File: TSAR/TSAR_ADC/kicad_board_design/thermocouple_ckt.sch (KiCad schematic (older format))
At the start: 75 parts, among them U3 AD8495, U4 AD8495, U5 AD8495, U6 AD8495, U7 ADA4062, U8 MCP3424T-E/ST, U9 LM358DR

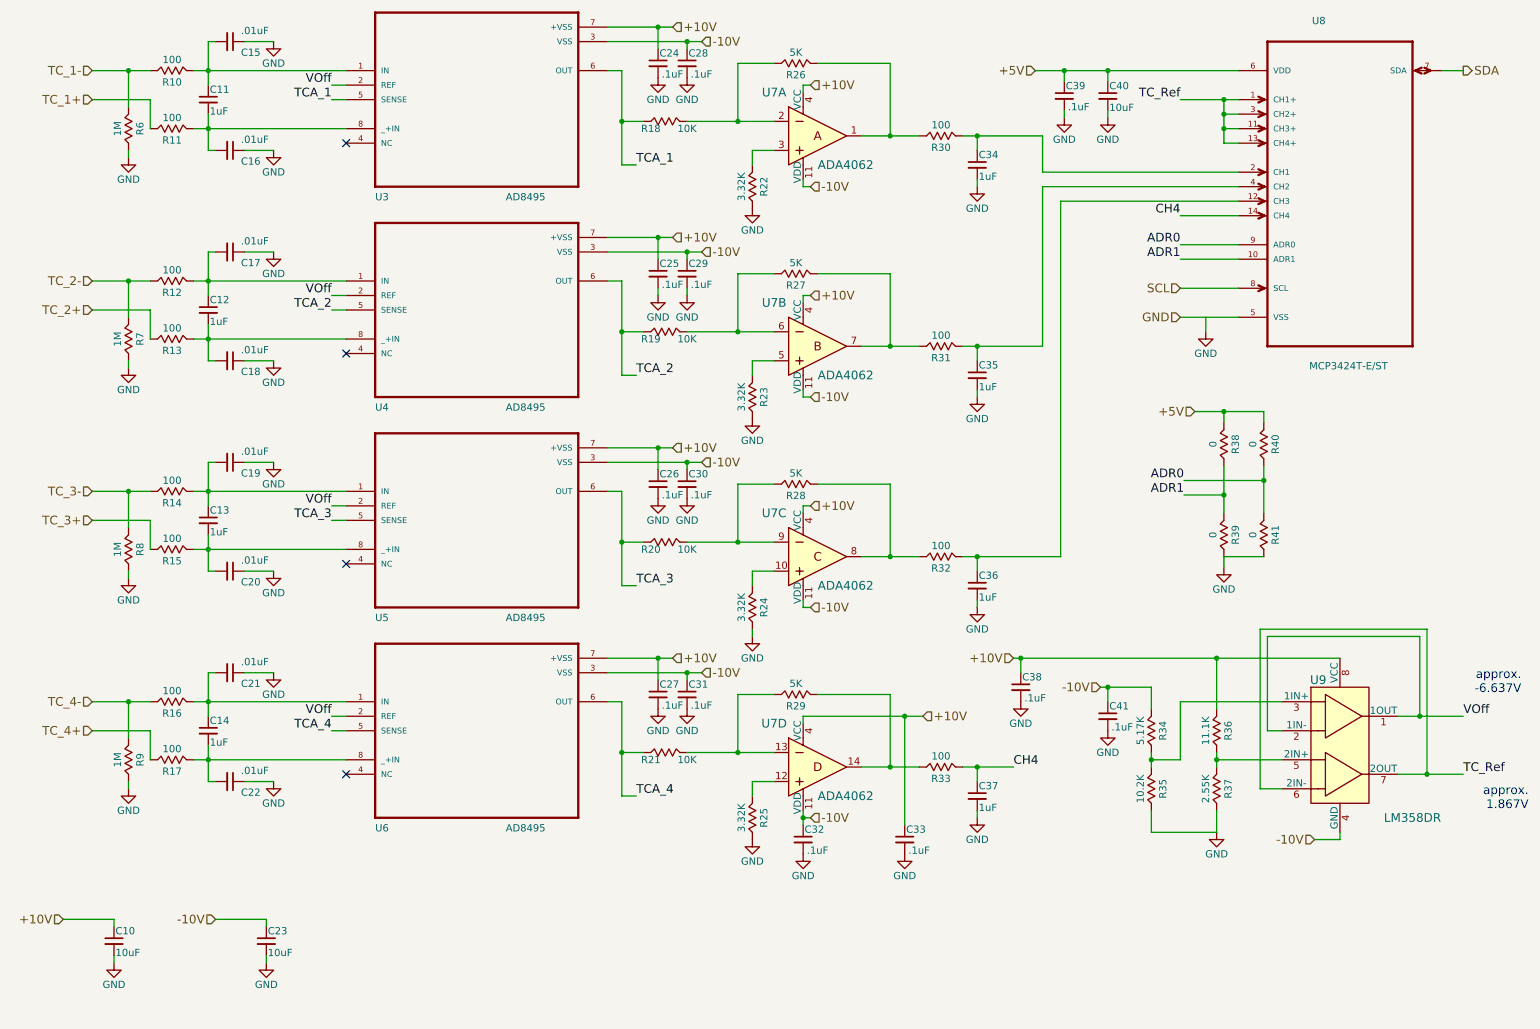
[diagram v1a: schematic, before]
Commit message: Simplify thermocouple signal chain for better worst case.
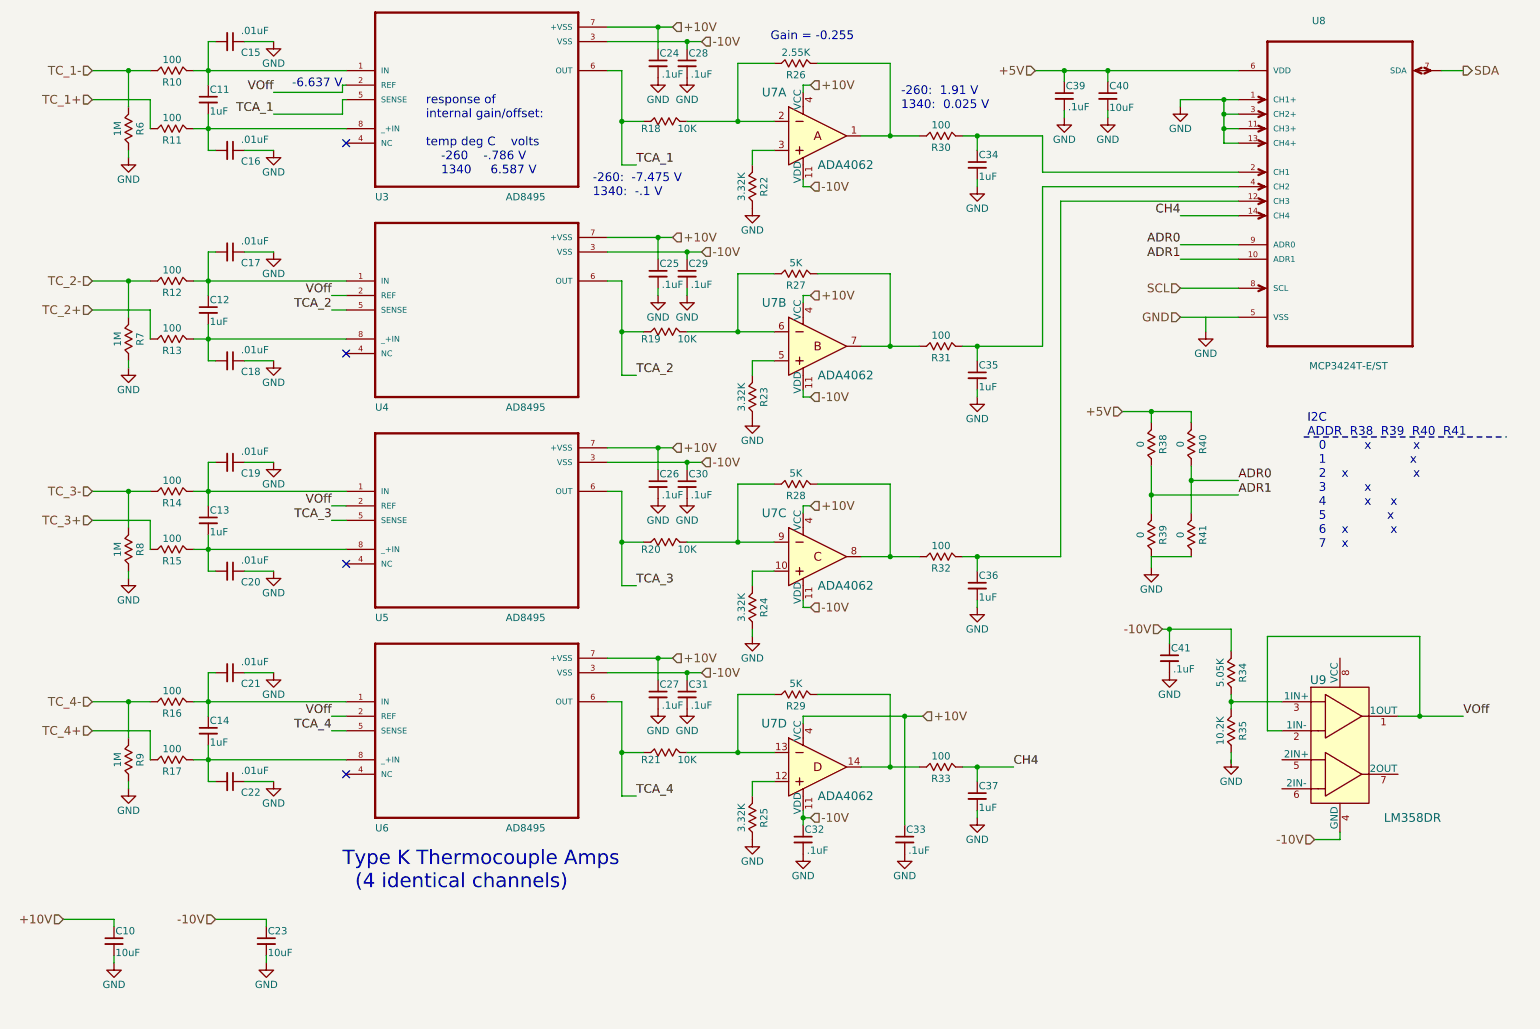
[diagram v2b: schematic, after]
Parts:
- removed C38: .1uF, Capacitors_SMD:C_0402, symbol C_Small
- removed R36: 11.1K, Resistors_SMD:R_0603_HandSoldering, symbol R
- removed R37: 2.55K, Resistors_SMD:R_0402, symbol R
- R26: value 5K -> 2.55K
- R34: value 5.17K -> 5.05K
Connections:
- net +10V: no longer U9.8 (VCC)
- net GND: now also U8.1 (CH1+), U8.11 (CH3+), U8.13 (CH4+), U8.3 (CH2+); no longer R35.2
- removed net TC_Ref: U8.1 (CH1+), U8.11 (CH3+), U8.13 (CH4+), U8.3 (CH2+), U9.6 (2IN-), U9.7 (2OUT)
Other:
- note added: "-260: -7.475 V\n1340: -.1 V"
- note added: "-260: 1.91 V\n1340: 0.025 V"
- note added: "-6.637 V"
- note added: "Gain = -0.255\n"
- note added: "I2C\nADDR R38 R39 R40 R41\n 0 x x\n 1 x\n 2 x x\n 3 x\n 4 x x\n 5 x\n 6 x x\n 7 x"
- note added: "Type K Thermocouple Amps\n (4 identical channels)"
- note added: "response of\ninternal gain/offset:\n\ntemp deg C volts\n -260 -.786 V\n 1340 6.587 V"
- note removed: "approx. \n1.867V"
- note removed: "approx.\n -6.637V"
- moved on the sheet: C41, R34, R35, R38, R39, R40, R41

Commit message: Incorporate review comments.  Improve U1 routing, general schematic comments.
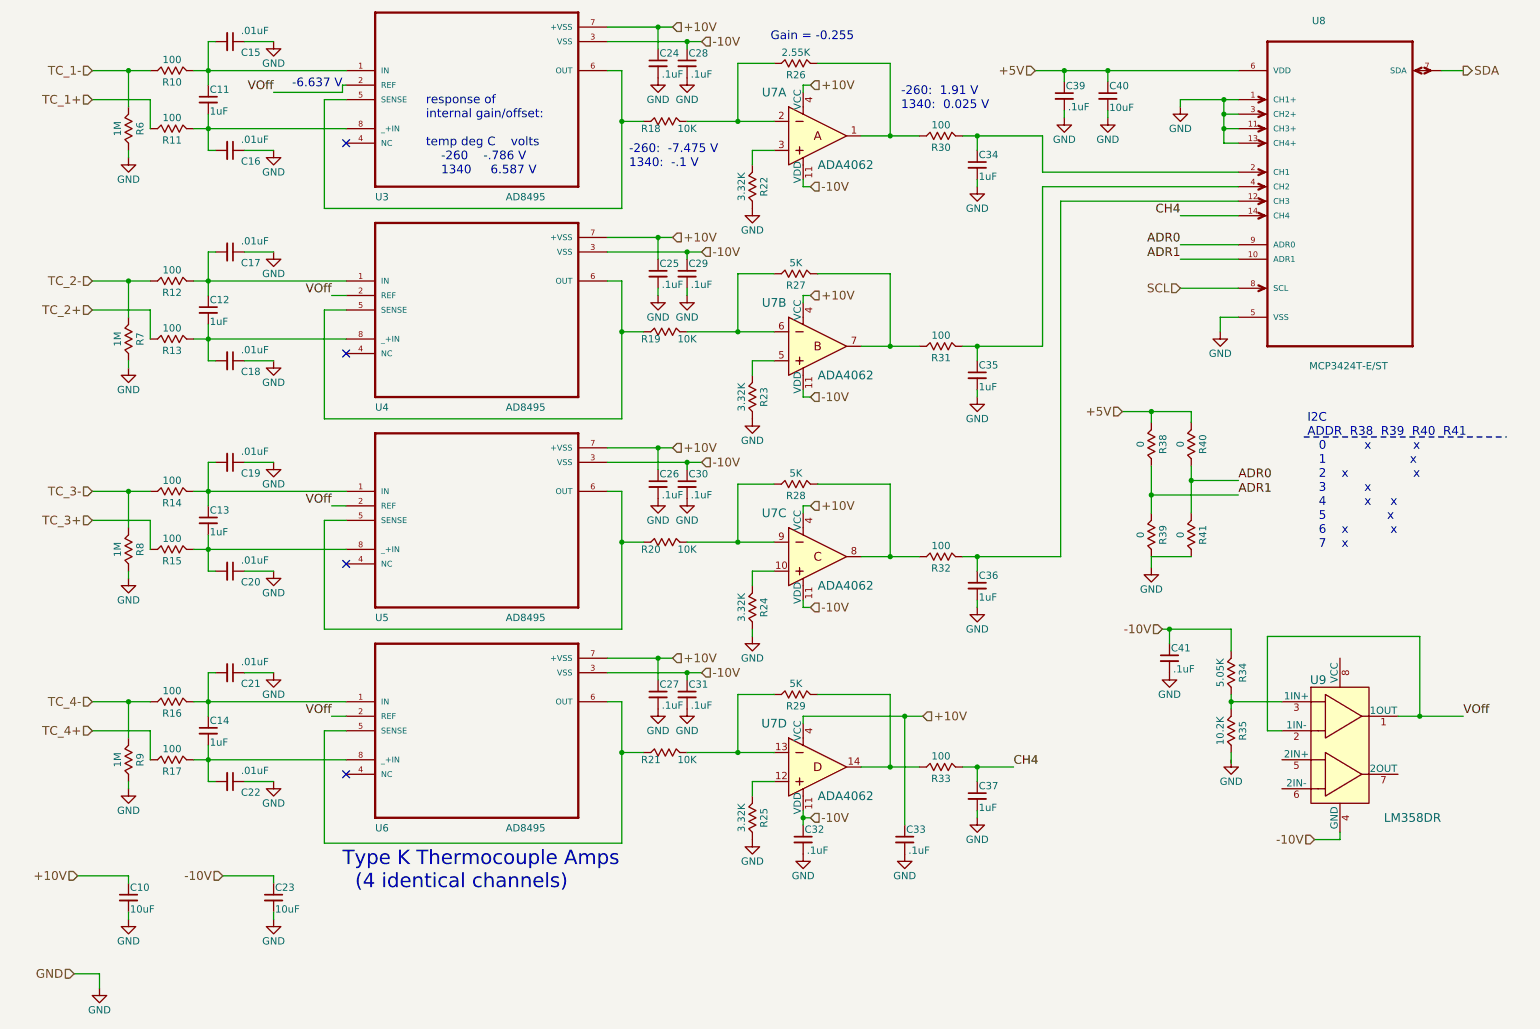
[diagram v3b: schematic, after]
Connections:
- net TCA_1: no longer names the net of R18.2, U3.5 (SENSE), U3.6 (OUT)
- net TCA_2: no longer names the net of R19.2, U4.5 (SENSE), U4.6 (OUT)
- net TCA_3: no longer names the net of R20.2, U5.5 (SENSE), U5.6 (OUT)
- net TCA_4: no longer names the net of R21.2, U6.5 (SENSE), U6.6 (OUT)
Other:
- moved on the sheet: C10, C23
